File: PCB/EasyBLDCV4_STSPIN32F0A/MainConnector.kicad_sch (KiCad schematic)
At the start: 8 parts, among them J1 10159560-A00221RLF

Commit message: Finished Schematic Assigned Footprints
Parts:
- added J2: STLINK-V3MINIE-EDGE, EasyBLDC:STLINK-V3MINIE-EDGE, symbol EasyBLDC:STLINK-V3MINIE-EDGE
- C1: renamed from C2; footprint (none) -> Capacitor_SMD:C_1206_3216Metric
- C2: renamed from C1; footprint (none) -> Capacitor_SMD:C_1206_3216Metric
- C3: renamed from C11; footprint (none) -> Capacitor_SMD:C_1206_3216Metric
- J1: footprint EasyBLDC:AMPHENOL_10159560-A00221RLF -> 10159560-A00221RLF:AMPHENOL_10159560-A00221RLF
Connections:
- net GND: now also J2.6 (GND)
- new net NRST: J2.9 (T_NRST)
- new net SWCLK: J2.4 (T_JCLK/T_SWCLK)
- new net SWDIO: J2.3 (T_JTMS/T_SWDIO)
- no-connect marks 0 -> 6
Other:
- note added: "Debug Connector"
- moved on the sheet: C1, C2, C3, H1, H2, H3, H4, J1

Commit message: Started Layout
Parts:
- J1: footprint 10159560-A00221RLF:AMPHENOL_10159560-A00221RLF -> EasyBLDC:AMPHENOL_10159560-A00221RLF
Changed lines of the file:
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@@
 			)
 		)
-		(property "Footprint" "10159560-A00221RLF:AMPHENOL_10159560-A00221RLF"
+		(property "Footprint" "EasyBLDC:AMPHENOL_10159560-A00221RLF"
 			(at 54.61 59.69 0)
 			(effects

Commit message: Design finished, ready for review
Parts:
- removed H1, H2, H3, H4: M2.5, MountingHole:MountingHole_2.7mm_M2.5_ISO7380, symbol Mechanical:MountingHole
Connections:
- net GND: no longer J1.S1 (SHIELD), J1.S2 (SHIELD__1)
- no-connect marks 6 -> 8
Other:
- note removed: "Standoffs"
- moved on the sheet: C1, C2, C3

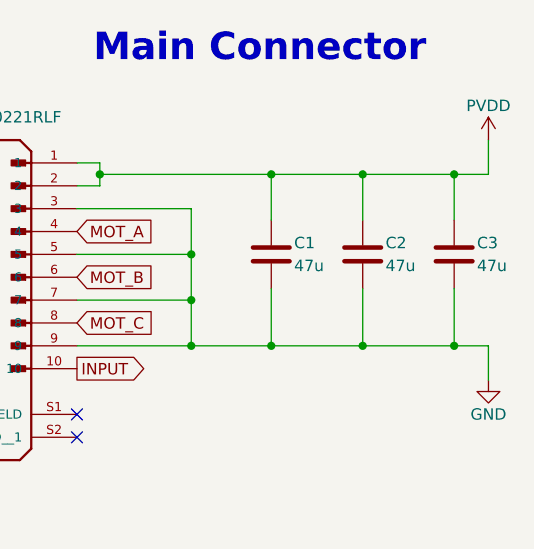
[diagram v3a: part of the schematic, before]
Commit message: Changed out 0201 resistors, production version
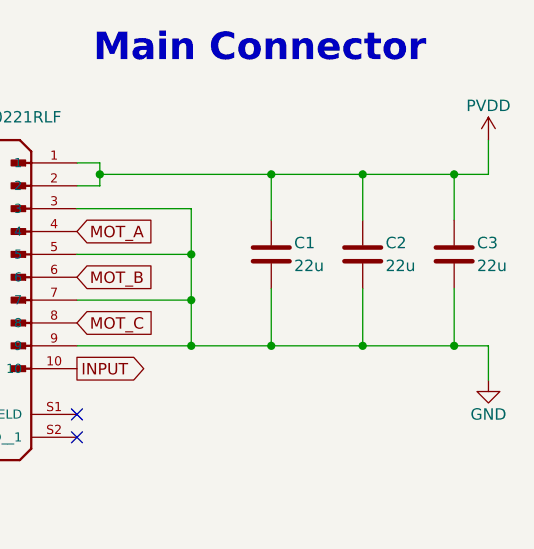
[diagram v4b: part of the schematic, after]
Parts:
- C1, C2, C3: value 47u -> 22u
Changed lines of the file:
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@@
 			)
 		)
-		(property "Value" "47u"
+		(property "Value" "22u"
 			(at 104.14 58.42 0)
 			(effects
@@
 			)
 		)
-		(property "Value" "47u"
+		(property "Value" "22u"
 			(at 93.98 58.42 0)
 			(effects
@@
 			)
 		)
-		(property "Value" "47u"
+		(property "Value" "22u"
 			(at 83.82 58.42 0)
 			(effects
